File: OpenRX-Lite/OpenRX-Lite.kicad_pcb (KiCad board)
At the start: 6 copper layers, 8.5 x 12.3 mm, 39 parts, among them U1 ESP32-C3FH4, U2 TLV75533PDQNR, U3 SX1281IMLTRT, X1 CJ17-400001010B20

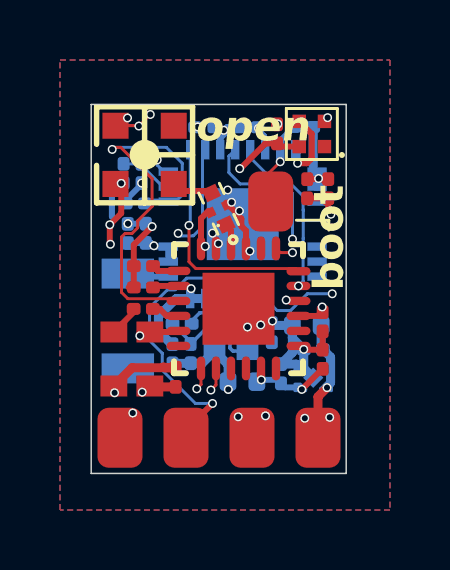
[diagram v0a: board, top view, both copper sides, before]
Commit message: switch to 0.2mm vias
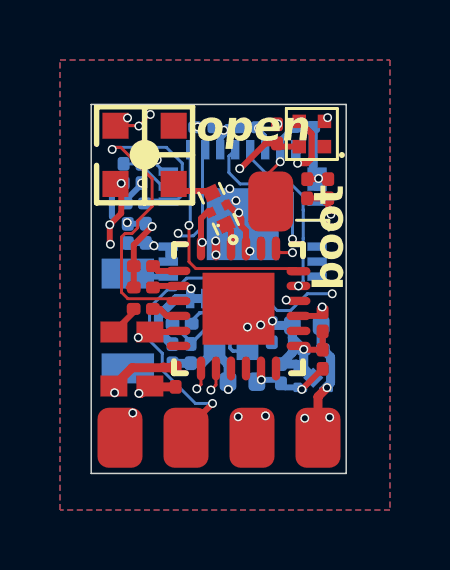
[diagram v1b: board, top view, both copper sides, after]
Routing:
- net GND: track 37.9 -> 38.6 mm
